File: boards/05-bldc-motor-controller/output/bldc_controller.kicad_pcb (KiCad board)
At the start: 2 copper layers, 80 x 100 mm, 55 parts, among them J1 Power Input, J2 Motor Output, J3 Hall Sensors, J4 SWD-6, Q1 IRLZ44N, Q2 IRLZ44N, Q3 IRLZ44N, Q4 IRLZ44N, Q5 IRLZ44N, Q6 IRLZ44N, U1 LM2596-5.0, U10 STM32G431K8Tx, U2 AMS1117-3.3, U3 DRV8301, Y1 8MHz

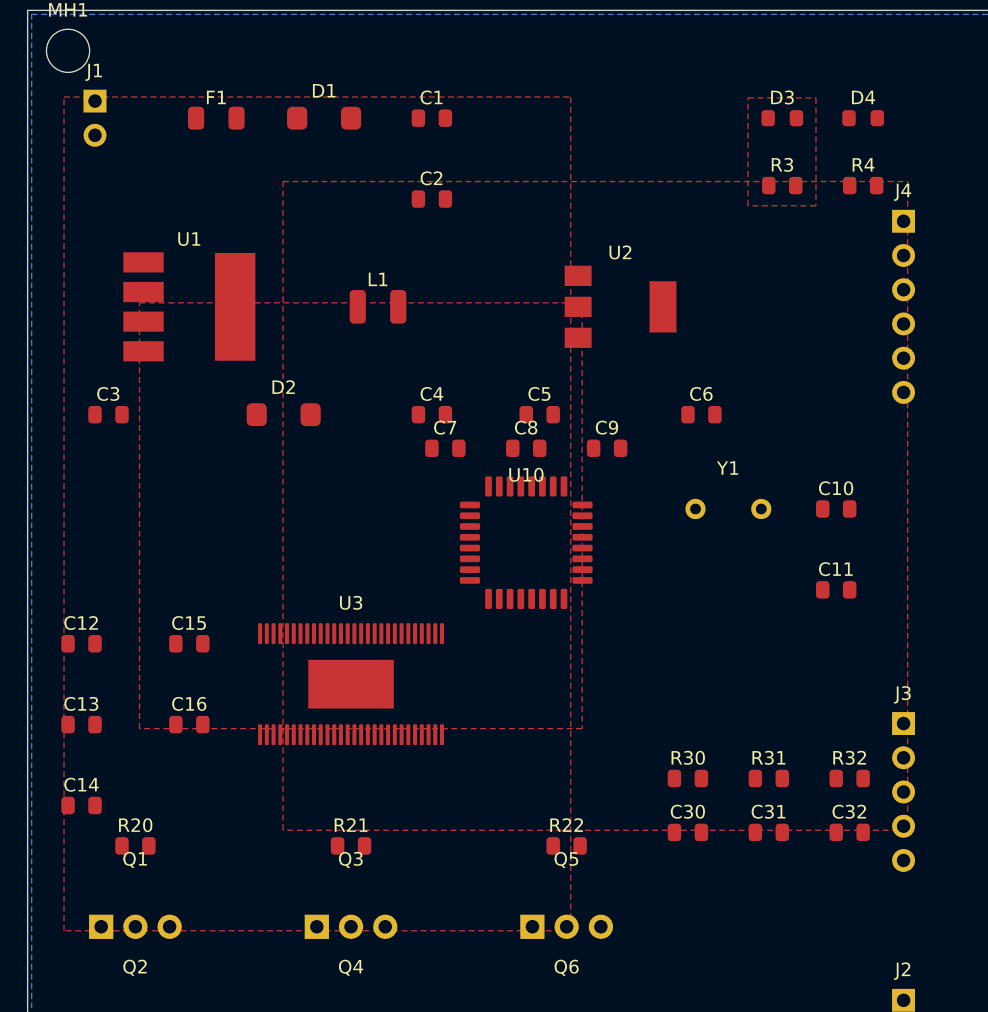
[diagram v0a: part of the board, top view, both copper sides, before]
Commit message: fix(boards/05): schematic-emit defects — LED polarity, BST chain, NCs, J4/U2/U1 pin maps, fuse nets (closes #3397)
Eliminates all 36 residual sync-netlist mismatches on board 05
(re-measured at 36 on current main; now 0 on both the unrouted and
routed committed artifacts). Per-defect triage:

1. LED polarity (D1/D3/D4) — REAL, PCB-side. generate_led_0805 mapped
   the anode to pad 1 (the LED_0805 footprint's cathode pad), and the
   PCB put the resistor on the anode side while the schematic
   LEDIndicator puts it on the cathode side; D1 (TVS) had its
   generate_diode_sma (net_a, net_k) args swapped, installing it
   backwards. Fixed the generator pad map and call sites; schematic
   gains PWR_LED/STATUS_LED labels (collision-aware stubs) so net
   names match the PCB.
2. Bootstrap chain (U3 BST pins) — REAL, both sides. U3.38/43/48 and
   cap C12-C14 high sides were DC-tied to +24V, defeating the
   bootstrap supply; the schematic's BootstrapCapacitorArray BST_x
   nets floated. Both sides now use BST_C/B/A nets (pin-to-cap-to-
   phase). Pins 29/53/54 (PVDD) stay +24V correctly; pin 52 (BST_BK)
   left as documented DC tie — no buck bootstrap cap exists on the
   board and it was not part of the 36.
3. U10 unused-pin NCs — REAL, PCB-side. Pads 8/9/10/21/22/25/27/28
   were tied to GND "for the autorouter" while the schematic marks
   them no-connect; pads now carry per-pad unconnected-(U10-...) nets
   matching KiCad's netlist-export convention.
4. J4 SWD pinout — REAL, schematic-side. Schematic emitted generic
   SWD-6 (GND/SWCLK/GND/NRST on pins 3-6, no SWO); now matches the
   PCB pad map (SWCLK/SWO/NRST/GND), restoring the MCU SWO trace pin.
   DebugHeader.connect_to_rails dropped (it would wire pin 3 — now
   SWCLK — onto the GND rail). J4 PCB position untouched (#3424).
5. U2 LDO pin swap — REAL, PCB-side. SOT-223 pads used 78xx-style
   (VIN/GND/VOUT); AMS1117 is GND/VOUT/VIN. Schematic was correct.
6. U1 buck pin swap — REAL, PCB-side. TO-263-5 pads 2/3/4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
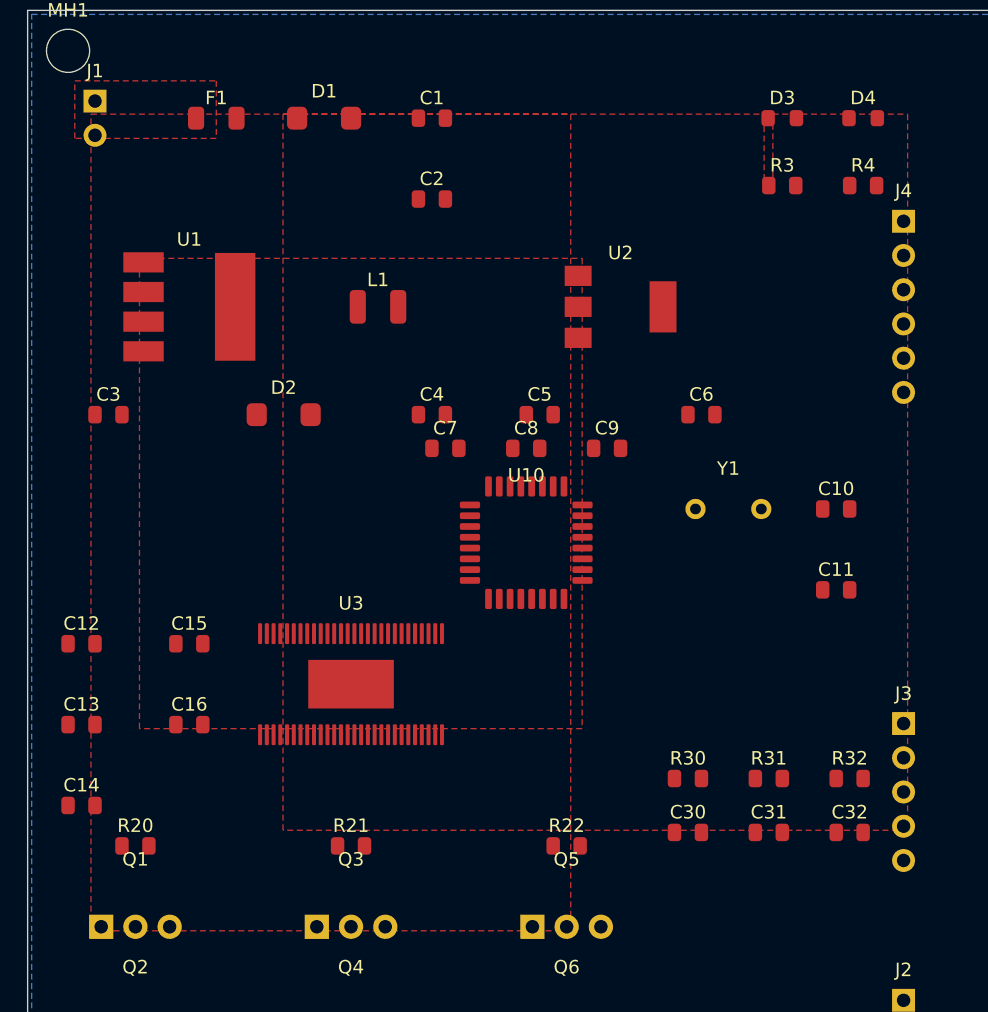
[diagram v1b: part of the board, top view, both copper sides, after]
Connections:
- C12 pad 1: +24V -> BST_C
- C13 pad 1: +24V -> BST_B
- C14 pad 1: +24V -> BST_A
- D1 pad 1: GND -> +24V
- D1 pad 2: +24V -> GND
- D3 pad 2: GND -> +3V3
- D4 pad 2: GND -> +3V3
- F1 pad 1: +24V -> VIN
- J1 pad 1: +24V -> VIN
- R3 pad 1: +3V3 -> PWR_LED
- R3 pad 2: PWR_LED -> GND
- R4 pad 1: +3V3 -> STATUS_LED
- R4 pad 2: STATUS_LED -> GND
- U1 pad 2: +5V -> SW_OUT
- U1 pad 3: SW_OUT -> GND
- U1 pad 4: GND -> +5V
- U10 pad 10: GND -> unconnected-(U10-PA5-Pad10)
- U10 pad 21: GND -> unconnected-(U10-PA11-Pad21)
- U10 pad 22: GND -> unconnected-(U10-PA12-Pad22)
- U10 pad 25: GND -> unconnected-(U10-PA15-Pad25)
- U10 pad 27: GND -> unconnected-(U10-PB4-Pad27)
- U10 pad 28: GND -> unconnected-(U10-PB5-Pad28)
- U10 pad 8: GND -> unconnected-(U10-PA3-Pad8)
- U10 pad 9: GND -> unconnected-(U10-PA4-Pad9)
- U2 pad 1: +5V -> GND
- U2 pad 2: GND -> +3V3
- U2 pad 3: +3V3 -> +5V
- U3 pad 38: +24V -> BST_C
- U3 pad 43: +24V -> BST_B
- U3 pad 48: +24V -> BST_A
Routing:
- added copper zone on F.Cu, net VIN
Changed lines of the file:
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@@
 	(net 39 "PWM_CH")
 	(net 40 "PWM_CL")
+	(net 41 "VIN")
+	(net 42 "BST_A")
+	(net 43 "BST_B")
+	(net 44 "BST_C")
+	(net 45 "unconnected-(U10-PA3-Pad8)")
+	(net 46 "unconnected-(U10-PA4-Pad9)")
+	(net 47 "unconnected-(U10-PA5-Pad10)")
+	(net 48 "unconnected-(U10-PA11-Pad21)")
+	(net 49 "unconnected-(U10-PA12-Pad22)")
+	(net 50 "unconnected-(U10-PA15-Pad25)")
+	(net 51 "unconnected-(U10-PB4-Pad27)")
+	(net 52 "unconnected-(U10-PB5-Pad28)")
 	(gr_rect
 		(start 100.0 100.0)
@@
 			(drill 1.0)
 			(layers "*.Cu" "*.Mask")
-			(net 1 "+24V")
+			(net 41 "VIN")
 		)
 		(pad "2" thru_hole oval
@@
 			(layers "F.Cu" "F.Paste" "F.Mask")
 			(roundrect_rratio 0.25)
-			(net 1 "+24V")
+			(net 41 "VIN")
 		)
 		(pad "2" smd roundrect
@@
 			(layers "F.Cu" "F.Paste" "F.Mask")
 			(roundrect_rratio 0.25)
-			(net 4 "GND")
+			(net 1 "+24V")
 		)
 		(pad "2" smd roundrect
@@
 			(layers "F.Cu" "F.Paste" "F.Mask")
 			(roundrect_rratio 0.25)
-			(net 1 "+24V")
+			(net 4 "GND")
 		)
 	)
@@
 			(size 3 1.5)
 			(layers "F.Cu" "F.Paste" "F.Mask")
-			(net 2 "+5V")
+			(net 31 "SW_OUT")
 		)
 		(pad "3" smd rect
@@
 			(size 3 1.5)
 			(layers "F.Cu" "F.Paste" "F.Mask")
-			(net 31 "SW_OUT")
+			(net 4 "GND")
 		)
 		(pad "4" smd rect
@@
 			(size 3 1.5)
 			(layers "F.Cu" "F.Paste" "F.Mask")
-			(net 4 "GND")
+			(net 2 "+5V")
 		)
 		(pad "5" smd rect
@@
 			(size 2 1.5)
 			(layers "F.Cu" "F.Paste" "F.Mask")
-			(net 2 "+5V")
+			(net 4 "GND")
 		)
 		(pad "2" smd rect
@@
 			(size 2 1.5)
 			(layers "F.Cu" "F.Paste" "F.Mask")
-			(net 4 "GND")
+			(net 3 "+3V3")
 		)
 		(pad "3" smd rect
@@
 			(size 2 1.5)
 			(layers "F.Cu" "F.Paste" "F.Mask")
-			(net 3 "+3V3")
+			(net 2 "+5V")
 		)
 		(pad "2" smd rect
@@
 			(size 2 3.8)
 			(layers "F.Cu" "F.Paste" "F.Mask")
-			(net 4 "GND")
+			(net 3 "+3V3")
 		)
 	)
@@
 			(layers "F.Cu" "F.Paste" "F.Mask")
 			(roundrect_rratio 0.25)
-			(net 1 "+24V")
+			(net 44 "BST_C")
 		)
 		(pad "39" smd roundrect
@@
 			(layers "F.Cu" "F.Paste" "F.Mask")
 			(roundrect_rratio 0.25)
-			(net 1 "+24V")
+			(net 43 "BST_B")
 		)
 		(pad "44" smd roundrect
@@
 			(layers "F.Cu" "F.Paste" "F.Mask")
 			(roundrect_rratio 0.25)
-			(net 1 "+24V")
+			(net 42 "BST_A")
 		)
 		(pad "49" smd roundrect
@@
 			(layers "F.Cu" "F.Paste" "F.Mask")
 			(roundrect_rratio 0.25)
-			(net 1 "+24V")
+			(net 44 "BST_C")
 		)
 		(pad "2" smd roundrect
@@
 			(layers "F.Cu" "F.Paste" "F.Mask")
 			(roundrect_rratio 0.25)
-			(net 1 "+24V")
+			(net 43 "BST_B")
 		)
 		(pad "2" smd roundrect
@@
 			(layers "F.Cu" "F.Paste" "F.Mask")
 			(roundrect_rratio 0.25)
-			(net 1 "+24V")
+			(net 42 "BST_A")
 		)
 		(pad "2" smd roundrect
@@
 			(layers "F.Cu" "F.Paste" "F.Mask")
 			(roundrect_rratio 0.25)
-			(net 4 "GND")
+			(net 45 "unconnected-(U10-PA3-Pad8)")
 		)
 		(pad "9" smd roundrect
@@
 			(layers "F.Cu" "F.Paste" "F.Mask")
 			(roundrect_rratio 0.25)
-			(net 4 "GND")
+			(net 46 "unconnected-(U10-PA4-Pad9)")
 		)
 		(pad "10" smd roundrect
@@
 			(layers "F.Cu" "F.Paste" "F.Mask")
 			(roundrect_rratio 0.25)
-			(net 4 "GND")
+			(net 47 "unconnected-(U10-PA5-Pad10)")
 		)
 		(pad "11" smd roundrect
@@
 			(layers "F.Cu" "F.Paste" "F.Mask")
 			(roundrect_rratio 0.25)
-			(net 4 "GND")
+			(net 48 "unconnected-(U10-PA11-Pad21)")
 		)
 		(pad "22" smd roundrect
@@
 			(layers "F.Cu" "F.Paste" "F.Mask")
 			(roundrect_rratio 0.25)
-			(net 4 "GND")
+			(net 49 "unconnected-(U10-PA12-Pad22)")
 		)
 		(pad "23" smd roundrect
@@
 			(layers "F.Cu" "F.Paste" "F.Mask")
 			(roundrect_rratio 0.25)
-			(net 4 "GND")
+			(net 50 "unconnected-(U10-PA15-Pad25)")
 		)
 		(pad "26" smd roundrect
@@
 			(layers "F.Cu" "F.Paste" "F.Mask")
 			(roundrect_rratio 0.25)
-			(net 4 "GND")
+			(net 51 "unconnected-(U10-PB4-Pad27)")
 		)
 		(pad "28" smd roundrect
@@
 			(layers "F.Cu" "F.Paste" "F.Mask")
 			(roundrect_rratio 0.25)
-			(net 4 "GND")
+			(net 52 "unconnected-(U10-PB5-Pad28)")
 		)
 		(pad "29" smd roundrect
@@
 			(layers "F.Cu" "F.Paste" "F.Mask")
 			(roundrect_rratio 0.25)
-			(net 3 "+3V3")
+			(net 29 "PWR_LED")
 		)
 		(pad "2" smd roundrect
@@
 			(layers "F.Cu" "F.Paste" "F.Mask")
 			(roundrect_rratio 0.25)
-			(net 29 "PWR_LED")
+			(net 4 "GND")
 		)
 	)
@@
 			(layers "F.Cu" "F.Paste" "F.Mask")
 			(roundrect_rratio 0.25)
-			(net 4 "GND")
+			(net 3 "+3V3")
 		)
 	)
@@
 			(layers "F.Cu" "F.Paste" "F.Mask")
 			(roundrect_rratio 0.25)
-			(net 3 "+3V3")
+			(net 30 "STATUS_LED")
 		)
 		(pad "2" smd roundrect
@@
 			(layers "F.Cu" "F.Paste" "F.Mask")
 			(roundrect_rratio 0.25)
-			(net 30 "STATUS_LED")
+			(net 4 "GND")
 		)
 	)
@@
 			(layers "F.Cu" "F.Paste" "F.Mask")
 			(roundrect_rratio 0.25)
-			(net 4 "GND")
+			(net 3 "+3V3")
 		)
 	)
@@
 		(layer "F.Cu")
 		(hatch edge 0.5)
-		(priority 4)
+		(priority 5)
 		(connect_pads (clearance 0.3)
 		)
@@
 		(fill yes (thermal_gap 0.3) (thermal_bridge_width 0.4)
 		)
-		(polygon (pts (xy 102.7 106.43) (xy 140.3 106.43) (xy 140.3 168.3) (xy 102.7 168.3))
+		(polygon (pts (xy 104.7 107.7) (xy 140.3 107.7) (xy 140.3 168.3) (xy 104.7 168.3))
 		)
 	)
@@
 		(layer "F.Cu")
 		(hatch edge 0.5)
-		(priority 3)
+		(priority 4)
 		(connect_pads (clearance 0.3)
 		)
@@
 		(fill yes (thermal_gap 0.3) (thermal_bridge_width 0.4)
 		)
-		(polygon (pts (xy 108.3 121.7) (xy 141.15 121.7) (xy 141.15 153.3) (xy 108.3 153.3))
+		(polygon (pts (xy 108.3 118.4) (xy 141.15 118.4) (xy 141.15 153.3) (xy 108.3 153.3))
 		)
 	)
@@
 		(layer "F.Cu")
 		(hatch edge 0.5)
-		(priority 2)
+		(priority 3)
 		(connect_pads (clearance 0.3)
 		)
@@
 		(fill yes (thermal_gap 0.3) (thermal_bridge_width 0.4)
 		)
-		(polygon (pts (xy 118.95 112.7) (xy 165.3 112.7) (xy 165.3 160.84) (xy 118.95 160.84))
+		(polygon (pts (xy 118.95 107.7) (xy 165.3 107.7) (xy 165.3 160.84) (xy 118.95 160.84))
 		)
 	)
@@
 		(layer "F.Cu")
 		(hatch edge 0.5)
-		(priority 1)
+		(priority 2)
 		(connect_pads (clearance 0.3)
 		)
@@
 		(fill yes (thermal_gap 0.3) (thermal_bridge_width 0.4)
 		)
-		(polygon (pts (xy 153.45 106.5) (xy 158.5 106.5) (xy 158.5 114.5) (xy 153.45 114.5))
-		)
-	)
+		(polygon (pts (xy 154.65 107.7) (xy 155.3 107.7) (xy 155.3 113.3) (xy 154.65 113.3))
+		)
+	)
+	(zone
+		(net 41)
+		(net_name "VIN")
+		(layer "F.Cu")
+		(hatch edge 0.5)
+		(priority 1)
+		(connect_pads (clearance 0.3)
+		)
+		(min_thickness 0.25)
+		(filled_areas_thickness no)
+		(fill yes (thermal_gap 0.3) (thermal_bridge_width 0.4)
+		)
+		(polygon (pts (xy 103.5 105.23) (xy 114 105.23) (xy 114 109.5) (xy 103.5 109.5))
+		)
+	)

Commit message: fix(boards/05): eliminate PWR_LED-to-+3V3 short via zone re-fill + classifier fix (refs #3513)
Review on PR #3526 found the new D3.1->R3.1 trace ran ~3.1mm INSIDE the
+3V3 F.Cu zone's stale filled_polygon -- the fill predated the trace and
was never regenerated, so the committed artifact shorted PWR_LED to +3V3
(D3 bypassed, R3 tying +3V3 to GND).  The DRC gate cannot see
segment-vs-foreign-zone-fill overlap (checker gap filed as #3527).

Fixes:

1. Re-filled all zones via `kct zones fill` (kicad-cli native fill) with
   the trace present.  The +3V3 fill now retreats around the trace with
   a 0.3005mm edge-to-edge gap (zone clearance 0.3mm; tier1 min 0.127mm).
   Only the +3V3 filled_polygon changed; all other fills were
   byte-identical.

2. Classifier fix (the real "drop PWR_LED from the pour list" change):
   PWR_LED matched the `^(...|PWR|POWER|...)` POWER prefix pattern, so
   BOTH design.py's create_zones_for_pcb AND `kct route`'s own auto-pour
   would recreate the geometrically-unfillable zone on every regen --
   a design.py-only exclusion cannot survive the route step.  The POWER
   pattern now carries `PWR(?!_?LED)` / `POWER(?!_?LED)` negative
   lookaheads; PWR_LED classifies SIGNAL, all other PWR*/POWER* nets are
   unchanged (PWR, PWR_5V, POWER_IN, VPWR, MCU_PWR, PWR_EN still POWER).

3. Removed the dead PWR_LED zone (uuid 7ba5fcbb) from the committed
   unrouted PCB so the artifact pair is consistent with the generator.

4. New `scripts/check_trace_vs_zone_fills.py`: point-in-polygon +
   min-clearance check of every segment against every foreign-net
   filled_polygon (the reviewer's method, generalized).  Until #3527
   lands in `kct check`, this is the only gate for this defect class.

5. Regression tests (tests/test_board_05_zones.py): PWR_LED must not
   classify POWER, the unrouted PCB must not carry a PWR_LED zone, and
   no PWR_LED segment centerline point may fall inside a foreign fill.

Regen verification: with the zone absent, `kct route` 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
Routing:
- removed copper zone on F.Cu, net PWR_LED
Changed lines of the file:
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@@
-	)
-	(zone
-		(net 29)
-		(net_name "PWR_LED")
-		(layer "F.Cu")
-		(hatch edge 0.5)
-		(priority 2)
-		(connect_pads (clearance 0.3)
-		)
-		(min_thickness 0.25)
-		(filled_areas_thickness no)
-		(fill yes (thermal_gap 0.3) (thermal_bridge_width 0.4)
-		)
-		(polygon (pts (xy 154.65 107.7) (xy 155.3 107.7) (xy 155.3 113.3) (xy 154.65 113.3))
-		)
 	)
 	(zone
